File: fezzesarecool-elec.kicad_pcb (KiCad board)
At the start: 2 copper layers, 65 x 56 mm, 62 parts, among them J1 Conn_sel, J14 Conn_LEDs, J15 Audio_input, J18 alim_jacky, J2 Conn_start, J3 CAN_conn, J4 CAN_conn, J5 Conn_01x02, J6 Conn_01x10, J7 alim_5V, P1 Conn_02x20_Odd_Even, Q1 NMOS-T252, Q2 NMOS-T252, Q3 NMOS-T252, U1 MCP2515-EST, U11 MC34152, U12 MC34152, U13 LM4991, U2 TCAN332, U3 SN74AHC1G08, Y1 Crystal_8MHz

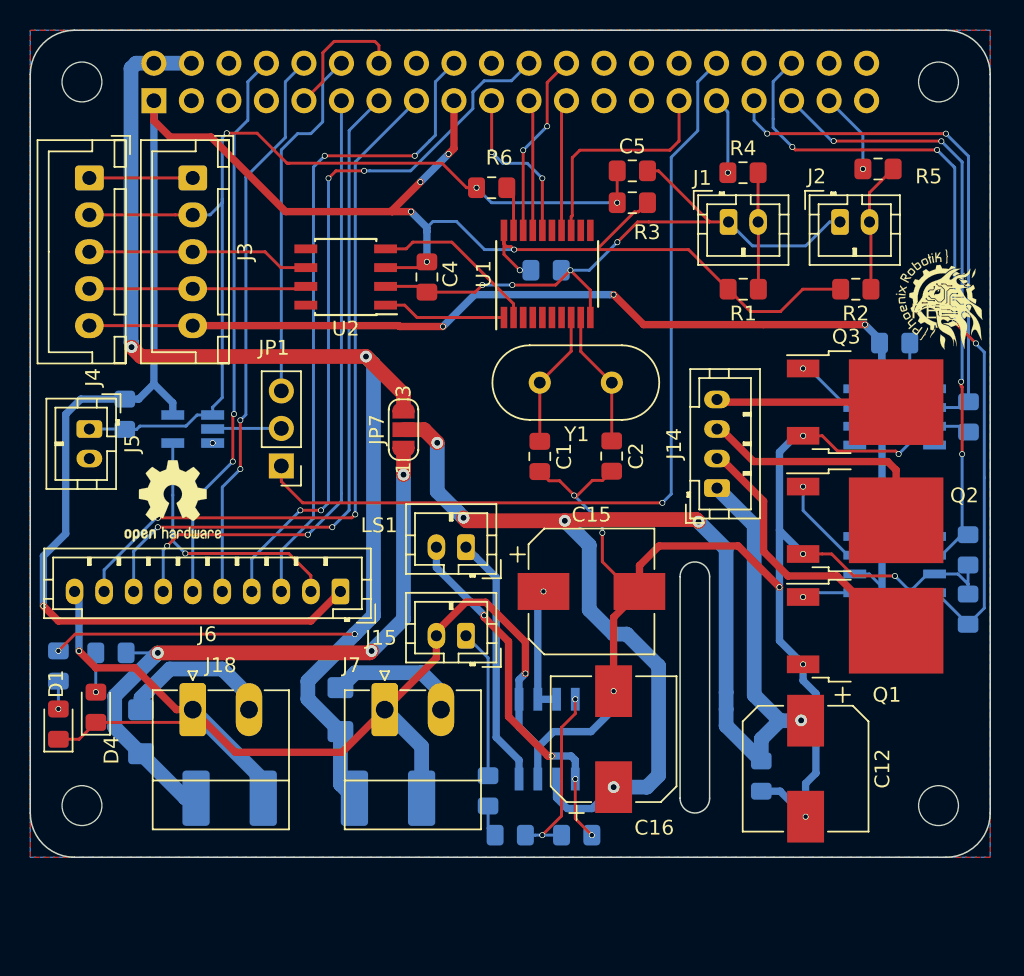
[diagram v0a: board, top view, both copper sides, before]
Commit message: add logos, fix phoenix phenix
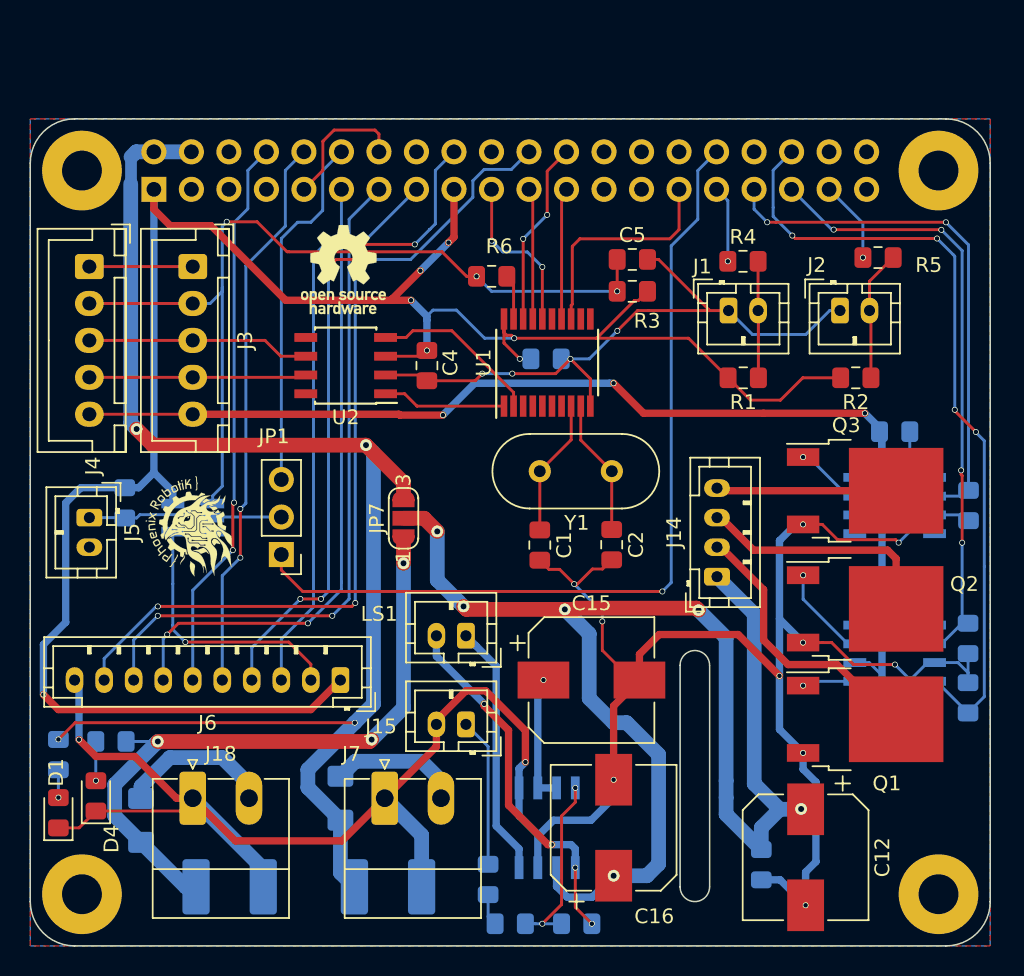
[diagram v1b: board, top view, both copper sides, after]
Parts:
- removed REF**: OSHW-Logo2_7.3x6mm_SilkScreen, Symbol:OSHW-Logo2_7.3x6mm_SilkScreen
- removed REF**: Logo_8,5mm, PhoenixRobotik:Logo_8,5mm
- added LOGO1: Logo_Open_Hardware_Small, PhenixRobotik:Logo_8,5mm, F.Cu at (210.8, 128.4)
- added LOGO2: Logo_Open_Hardware_Small, Symbol:OSHW-Logo_5.7x6mm_SilkScreen, F.Cu at (221.2, 110.2)
- added LOGO3: Logo_Open_Hardware_Small, Symbol:KiCad-Logo2_6mm_SilkScreen, B.Cu at (253.2, 145.6)
- H1, H2, H3, H4: value MountingHole -> MountingHole_Pad; footprint MountingHole:MountingHole_2.7mm_M2.5 -> MountingHole:MountingHole_2.7mm_M2.5_Pad
- moved C1 6.00 mm to (234.5, 128.9)
- moved C10 6.00 mm to (258.7, 140.3)
- moved C11 6.00 mm to (258.5, 121.2)
- moved C12 6.00 mm to (252.5, 150.0)
- moved C13 6.00 mm to (249.5, 150.5)
- moved C14 6.00 mm to (231.0, 151.5)
- moved C15 6.00 mm to (238.0, 138.0)
- moved C16 6.00 mm to (239.5, 148.0)
- moved C3 6.00 mm to (234.9, 116.2)
- moved C4 6.00 mm to (226.9, 116.7)
- moved C5 6.00 mm to (240.8, 109.5)
- moved D1 6.00 mm to (201.9, 147.0)
- moved D2 6.00 mm to (224.2, 152.0)
- moved D4 6.00 mm to (204.4, 145.8)
- moved D6 6.00 mm to (213.5, 152.0)
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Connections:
- H1 pad 1: (no net) -> GND
- H2 pad 1: (no net) -> GND
- H3 pad 1: (no net) -> GND
- H4 pad 1: (no net) -> GND
- P1 pad 16: (no net) -> /GPIO23(GEN4)
- P1 pad 26: (no net) -> /GPIO7(SPI1_CE_N)
- P1 pad 27: (no net) -> /ID_SD
- P1 pad 28: (no net) -> /ID_SC
- P1 pad 3: (no net) -> /GPIO2(SDA1)
- P1 pad 38: (no net) -> /GPIO20(SPI1_MOSI)
- P1 pad 40: (no net) -> /GPIO21(SPI1_SCK)
- P1 pad 5: (no net) -> /GPIO3(SCL1)
- P1 pad 7: (no net) -> /GPIO4(GCLK)
- U1 pad 11: (no net) -> Net-(U1-Pad11)
- U1 pad 12: (no net) -> Net-(U1-Pad12)
- U1 pad 15: (no net) -> Net-(U1-Pad15)
- U1 pad 3: (no net) -> Net-(U1-Pad3)
- U1 pad 4: (no net) -> Net-(U1-Pad4)
- U1 pad 5: (no net) -> Net-(U1-Pad5)
- U1 pad 6: (no net) -> Net-(U1-Pad6)
- U1 pad 7: (no net) -> Net-(U1-Pad7)
- U11 pad 1: (no net) -> Net-(U11-Pad1)
- U11 pad 8: (no net) -> Net-(U11-Pad8)
- U12 pad 1: (no net) -> Net-(U12-Pad1)
- U12 pad 5: (no net) -> Net-(U12-Pad5)
- U12 pad 8: (no net) -> Net-(U12-Pad8)
- U2 pad 5: (no net) -> Net-(U2-Pad5)
- U2 pad 8: (no net) -> Net-(U2-Pad8)

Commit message: cleanup
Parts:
- R4, R5: moved to B.Cu
- moved F3 7.75 mm to (214.6, 144.4), turned to 180 degrees
- moved R2 7.32 mm to (262.6, 114.6), turned to 270 degrees
- moved F1 6.60 mm to (227.4, 144.4), turned to 180 degrees
- moved R1 5.73 mm to (253.2, 114.6), turned to 270 degrees
- moved R16 3.11 mm to (204.2, 145.0), turned to 270 degrees
- moved D6 2.77 mm to (210.8, 152.6), turned to 180 degrees
- moved J2 2.17 mm to (257.0, 113.0)
- moved R13 1.96 mm to (201.8, 145.0)
- moved J18 1.80 mm to (211.0, 147.8)
- moved J7 1.80 mm to (224.0, 147.8)
- moved D4 1.19 mm to (204.2, 147.0)
- moved D2 0.87 mm to (223.6, 152.6), turned to 180 degrees
- moved R5 0.63 mm to (258.0, 109.6)
- moved R4 0.34 mm to (248.6, 109.6)
- moved J1 0.32 mm to (247.6, 113.0)
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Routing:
- net GND: track 253.9 -> 232.9 mm
- net +5VD: track 96.3 -> 79.8 mm, vias 6 -> 5
- net Net-(F3-Pad1): track 10.6 -> 3.93 mm
- net +3V3: track 142.7 -> 148.8 mm
- net Net-(F1-Pad1): track 8.96 -> 3.85 mm
- net Net-(D4-Pad2): track 2.66 -> 0.00 mm
- net /GPIO16: track 53.7 -> 51.5 mm, vias 4 -> 2
- net Net-(D1-Pad2): track 1.89 -> 0.00 mm
- net /GPIO8(SPI0_CE_N): track 12.5 -> 14.3 mm, vias 2 -> 0
- net /GPIO13(PWM1): track 35.9 -> 34.3 mm, vias 2 -> 0
- net Net-(J2-Pad2): track 8.84 -> 7.25 mm
- net Net-(D6-Pad1): track 45.1 -> 43.9 mm
- net /GPIO19(SPI1_MISO): track 41.6 -> 42.3 mm, vias 4 -> 2
- net Net-(J1-Pad2): track 7.90 -> 7.25 mm
- net /GPIO6: track 5.19 -> 5.29 mm, vias 1 -> 0
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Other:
- board text added: "Alim5V"
- board text added: "AlimJacky"
- board text added: "AudioIn"
- board text added: "AudioOut"
- board text added: "CAN"
- board text added: "LEDs"
- board text added: "Reset"
- board text added: "SWD + UART"
- board text added: "Select"
- board text added: "Start"

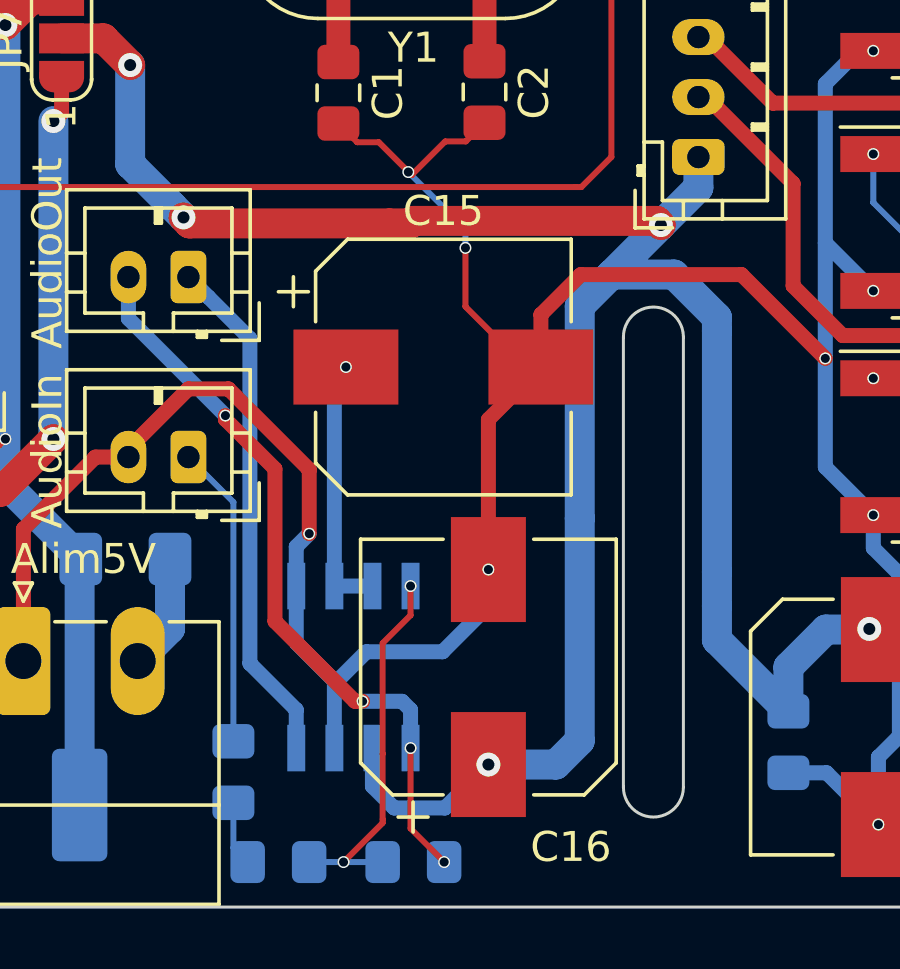
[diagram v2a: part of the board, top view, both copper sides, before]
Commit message: Changed audio capacitors footprint
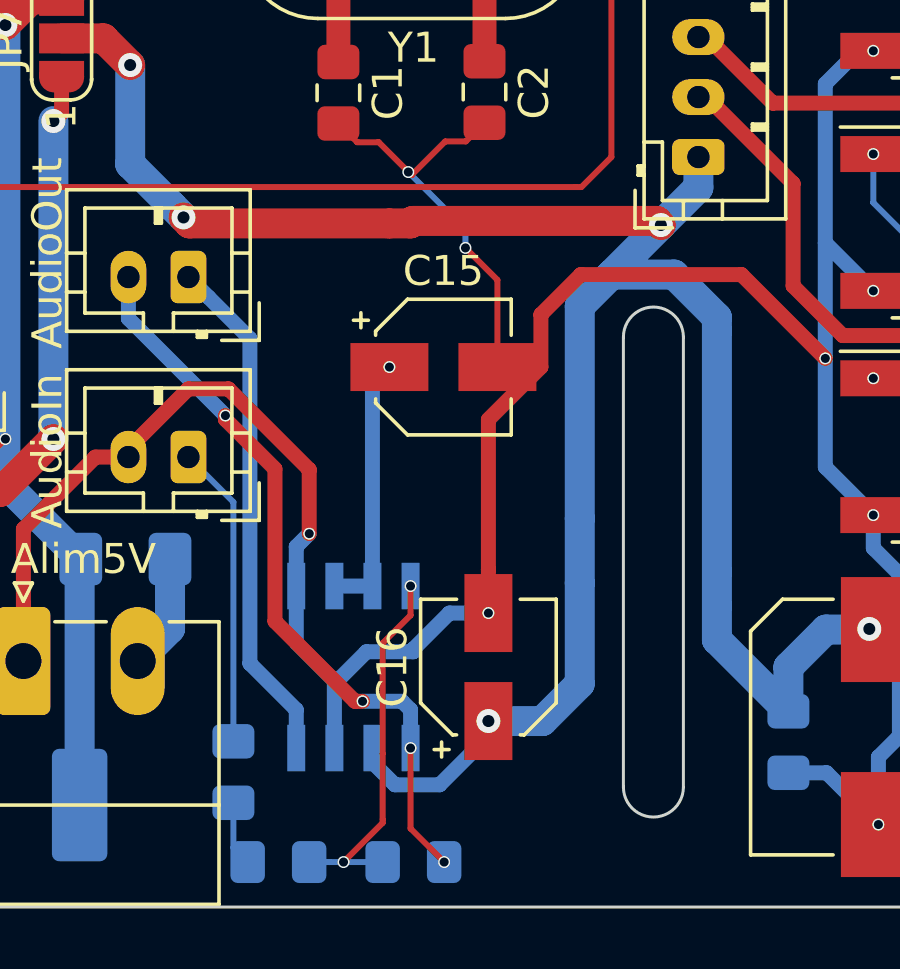
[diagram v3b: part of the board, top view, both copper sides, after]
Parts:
- C1, C2: value C -> 26p
- C10, C11, C3, C4: value C -> 100n
- C15, C16: footprint Capacitor_SMD:CP_Elec_8x10 -> Capacitor_SMD:CP_Elec_4x5.4
- C5: value C -> cf. doc p55
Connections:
- P1 pad 16: /GPIO23(GEN4) -> (no net)
- P1 pad 26: /GPIO7(SPI1_CE_N) -> (no net)
- P1 pad 27: /ID_SD -> (no net)
- P1 pad 28: /ID_SC -> (no net)
- P1 pad 3: /GPIO2(SDA1) -> (no net)
- P1 pad 38: /GPIO20(SPI1_MOSI) -> (no net)
- P1 pad 40: /GPIO21(SPI1_SCK) -> (no net)
- P1 pad 5: /GPIO3(SCL1) -> (no net)
- P1 pad 7: /GPIO4(GCLK) -> (no net)
- U1 pad 11: Net-(U1-Pad11) -> (no net)
- U1 pad 12: Net-(U1-Pad12) -> (no net)
- U1 pad 15: Net-(U1-Pad15) -> (no net)
- U1 pad 3: Net-(U1-Pad3) -> (no net)
- U1 pad 4: Net-(U1-Pad4) -> (no net)
- U1 pad 5: Net-(U1-Pad5) -> (no net)
- U1 pad 6: Net-(U1-Pad6) -> (no net)
- U1 pad 7: Net-(U1-Pad7) -> (no net)
- U11 pad 1: Net-(U11-Pad1) -> (no net)
- U11 pad 8: Net-(U11-Pad8) -> (no net)
- U12 pad 1: Net-(U12-Pad1) -> (no net)
- U12 pad 5: Net-(U12-Pad5) -> (no net)
- U12 pad 8: Net-(U12-Pad8) -> (no net)
- U2 pad 5: Net-(U2-Pad5) -> (no net)
- U2 pad 8: Net-(U2-Pad8) -> (no net)
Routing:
- net +5VD: track 79.8 -> 77.9 mm

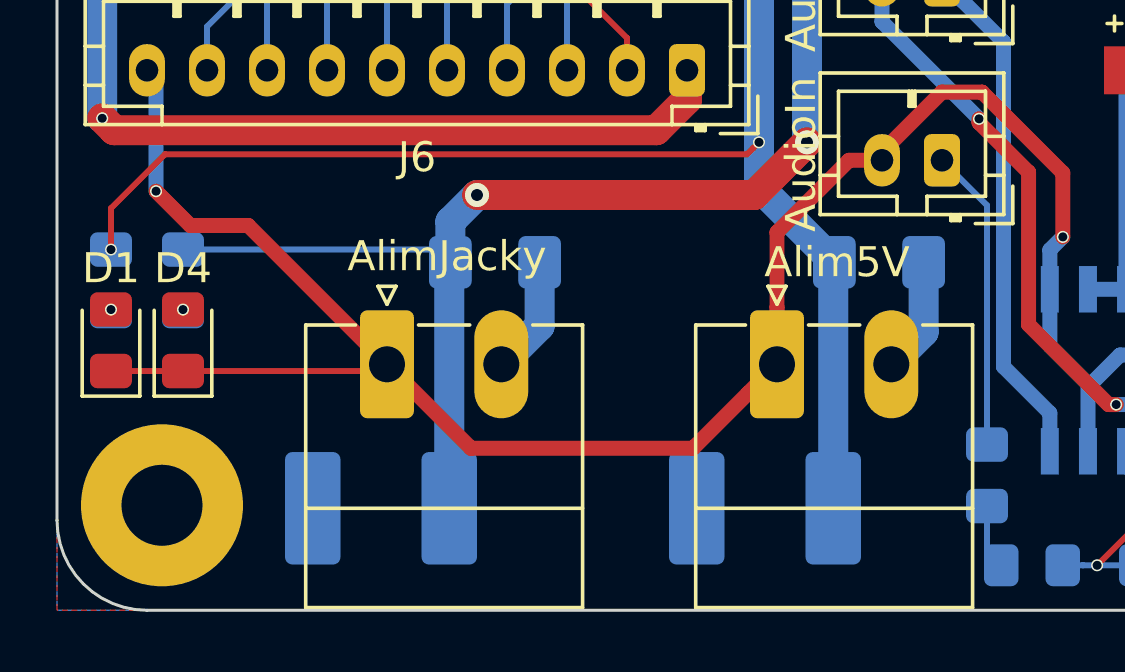
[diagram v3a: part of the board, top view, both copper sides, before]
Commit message: Changed fuse footprint
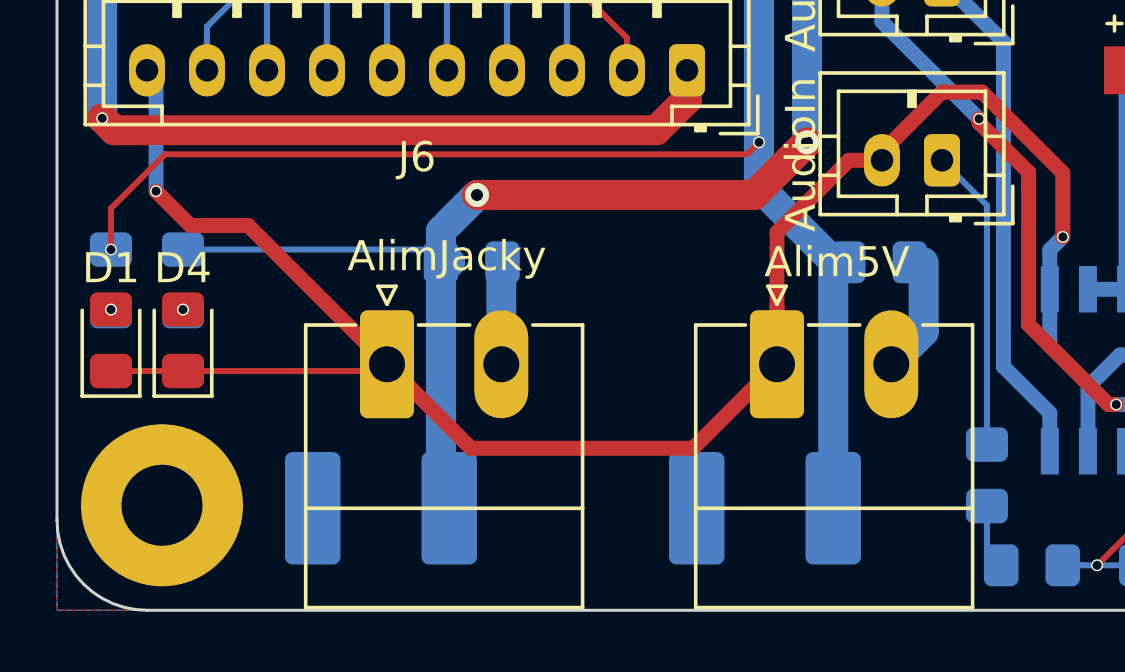
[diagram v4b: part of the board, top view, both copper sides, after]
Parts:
- F1, F3: footprint Fuse:Fuse_1206_3216Metric_Pad1.42x1.75mm_HandSolder -> Fuse:Fuse_0805_2012Metric_Pad1.15x1.40mm_HandSolder
- moved F3 0.78 mm to (213.8, 144.4)
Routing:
- net Net-(D6-Pad1): track 43.9 -> 45.7 mm
- net Net-(F3-Pad1): track 3.93 -> 3.42 mm
